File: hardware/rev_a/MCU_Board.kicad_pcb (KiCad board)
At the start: 2 copper layers, 30 x 55 mm, 28 parts, among them J1 ST-Link, J2 Conn_01x08, J3 Bus, J4 Conn_01x08, J5 Conn_02x07_Odd_Even, SW1 nRST, U1 STM32F042K6Tx, U3 SN65HVD230, U4 LP2985-3.3, Y1 8Mhz

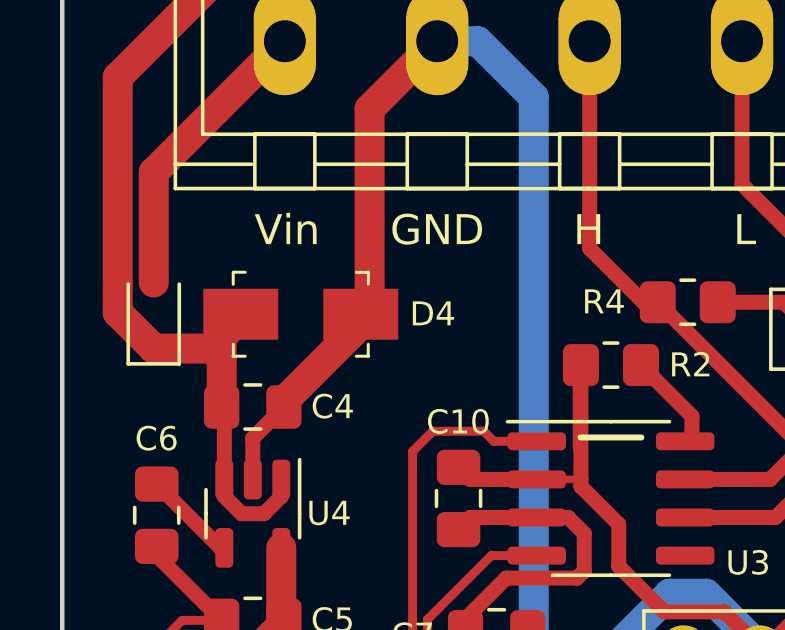
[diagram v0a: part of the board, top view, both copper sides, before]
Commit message: Remove the dependancy with external libraries, the TVS diode is now using the default symbol and a custom footprint
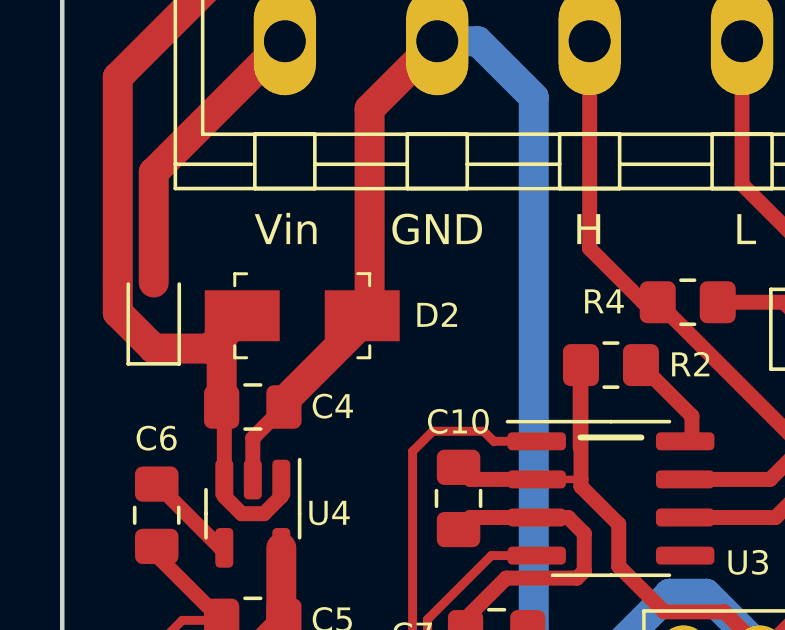
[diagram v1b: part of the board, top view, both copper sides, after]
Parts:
- removed D4: SMBJ12CA-E3/52, custom:DO-214AA
- added D2: SMBJ12CA-E3/52, custom:DO-214AA, F.Cu at (74.2, 113.2)
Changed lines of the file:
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@@
     )
-  )
-  (footprint "custom:DO-214AA" (layer "F.Cu")
-    (at 74.2 113.2)
-    (property "Sheetfile" "MCU_Board.kicad_sch")
-    (property "Sheetname" "")
-    (property "ki_description" "TVS DIODE 3.3V 14.1V SOD523")
-    (property "ki_keywords" "ESD5Z3.3T1GOSCT-ND")
-    (attr smd)
-    (fp_text reference "D4" (at 4.4 0) (layer "F.SilkS")
-        (effects (font (size 0.8 0.8) (thickness 0.15)))
-    )
-    (fp_text value "SMBJ12CA-E3/52" (at 0 2.45) (layer "F.Fab")
-        (effects (font (size 1 1) (thickness 0.15)))
-    )
-    (fp_text user "${REFERENCE}" (at 0.40894 0) (layer "F.Fab")
-        (effects (font (size 0.75 0.75) (thickness 0.075)))
-    )
-    (fp_line (start -2.25 -1.4) (end -2.25 -1)
-      (stroke (width 0.1) (type solid)) (layer "F.SilkS"))
-    (fp_line (start -2.25 -1.4) (end -1.85 -1.4)
-      (stroke (width 0.1) (type solid)) (layer "F.SilkS"))
-    (fp_line (start -2.25 1.4) (end -2.25 1)
-      (stroke (width 0.1) (type solid)) (layer "F.SilkS"))
-    (fp_line (start -2.25 1.4) (end -1.85 1.4)
-      (stroke (width 0.1) (type solid)) (layer "F.SilkS"))
-    (fp_line (start 2.25 -1.4) (end 1.85 -1.4)
-      (stroke (width 0.1) (type solid)) (layer "F.SilkS"))
-    (fp_line (start 2.25 -1.4) (end 2.25 -1)
-      (stroke (width 0.1) (type solid)) (layer "F.SilkS"))
-    (fp_line (start 2.25 1.4) (end 1.85 1.4)
-      (stroke (width 0.1) (type solid)) (layer "F.SilkS"))
-    (fp_line (start 2.25 1.4) (end 2.25 1)
-      (stroke (width 0.1) (type solid)) (layer "F.SilkS"))
-    (fp_line (start -3.5 -1.55) (end -3.5 1.55)
-      (stroke (width 0.05) (type solid)) (layer "F.CrtYd"))
-    (fp_line (start -3.5 -1.55) (end 3.5 -1.55)
-      (stroke (width 0.05) (type solid)) (layer "F.CrtYd"))
-    (fp_line (start -3.5 1.55) (end 3.5 1.55)
-      (stroke (width 0.05) (type solid)) (layer "F.CrtYd"))
-    (fp_line (start 3.5 -1.55) (end 3.5 1.55)
-      (stroke (width 0.05) (type solid)) (layer "F.CrtYd"))
-    (fp_line (start -2.15 -1.3) (end 2.15 -1.3)
-      (stroke (width 0.1) (type solid)) (layer "F.Fab"))
-    (fp_line (start -2.15 1.3) (end 2.15 1.3)
-      (stroke (width 0.1) (type solid)) (layer "F.Fab"))
-    (fp_line (start -1.44018 1.30048) (end -1.36398 1.30048)
-      (stroke (width 0.1) (type solid)) (layer "F.Fab"))
-    (fp_line (start -1.36144 -1.30048) (end -1.44018 -1.30048)
-      (stroke (width 0.1) (type solid)) (layer "F.Fab"))
-    (pad "A" smd rect (at 2 0) (size 2.5 1.7) (layers "F.Cu" "F.Paste" "F.Mask")
-      (net 1 "GND") (pintype "bidirectional"))
-    (pad "K" smd rect (at -2 0) (size 2.5 1.7) (layers "F.Cu" "F.Paste" "F.Mask")
-      (net 3 "/VIN") (pintype "bidirectional"))
   )
   (footprint "Diode_SMD:D_SOD-323F" (layer "F.Cu")
@@
     )
   )
+  (footprint "custom:DO-214AA" (layer "F.Cu")
+    (at 74.25 113.25 180)
+    (property "Sheetfile" "MCU_Board.kicad_sch")
+    (property "Sheetname" "")
+    (property "ki_description" "Bidirectional transient-voltage-suppression diode")
+    (property "ki_keywords" "diode TVS thyrector")
+    (attr smd)
+    (fp_text reference "D2" (at -4.5 0) (layer "F.SilkS")
+        (effects (font (size 0.8 0.8) (thickness 0.15)))
+    )
+    (fp_text value "SMBJ12CA-E3/52" (at 0 2.45) (layer "F.Fab")
+        (effects (font (size 1 1) (thickness 0.15)))
+    )
+    (fp_text user "${REFERENCE}" (at 0.40894 0) (layer "F.Fab")
+        (effects (font (size 0.75 0.75) (thickness 0.075)))
+    )
+    (fp_line (start -2.25 -1.4) (end -2.25 -1)
+      (stroke (width 0.1) (type solid)) (layer "F.SilkS"))
+    (fp_line (start -2.25 -1.4) (end -1.85 -1.4)
+      (stroke (width 0.1) (type solid)) (layer "F.SilkS"))
+    (fp_line (start -2.25 1.4) (end -2.25 1)
+      (stroke (width 0.1) (type solid)) (layer "F.SilkS"))
+    (fp_line (start -2.25 1.4) (end -1.85 1.4)
+      (stroke (width 0.1) (type solid)) (layer "F.SilkS"))
+    (fp_line (start 2.25 -1.4) (end 1.85 -1.4)
+      (stroke (width 0.1) (type solid)) (layer "F.SilkS"))
+    (fp_line (start 2.25 -1.4) (end 2.25 -1)
+      (stroke (width 0.1) (type solid)) (layer "F.SilkS"))
+    (fp_line (start 2.25 1.4) (end 1.85 1.4)
+      (stroke (width 0.1) (type solid)) (layer "F.SilkS"))
+    (fp_line (start 2.25 1.4) (end 2.25 1)
+      (stroke (width 0.1) (type solid)) (layer "F.SilkS"))
+    (fp_line (start -3.5 -1.55) (end -3.5 1.55)
+      (stroke (width 0.05) (type solid)) (layer "F.CrtYd"))
+    (fp_line (start -3.5 -1.55) (end 3.5 -1.55)
+      (stroke (width 0.05) (type solid)) (layer "F.CrtYd"))
+    (fp_line (start -3.5 1.55) (end 3.5 1.55)
+      (stroke (width 0.05) (type solid)) (layer "F.CrtYd"))
+    (fp_line (start 3.5 -1.55) (end 3.5 1.55)
+      (stroke (width 0.05) (type solid)) (layer "F.CrtYd"))
+    (fp_line (start -2.15 -1.3) (end 2.15 -1.3)
+      (stroke (width 0.1) (type solid)) (layer "F.Fab"))
+    (fp_line (start -2.15 1.3) (end 2.15 1.3)
+      (stroke (width 0.1) (type solid)) (layer "F.Fab"))
+    (fp_line (start -1.44018 1.30048) (end -1.36398 1.30048)
+      (stroke (width 0.1) (type solid)) (layer "F.Fab"))
+    (fp_line (start -1.36144 -1.30048) (end -1.44018 -1.30048)
+      (stroke (width 0.1) (type solid)) (layer "F.Fab"))
+    (pad "1" smd rect (at -2 0 180) (size 2.5 1.7) (layers "F.Cu" "F.Paste" "F.Mask")
+      (net 1 "GND") (pinfunction "A1") (pintype "passive"))
+    (pad "2" smd rect (at 2 0 180) (size 2.5 1.7) (layers "F.Cu" "F.Paste" "F.Mask")
+      (net 3 "/VIN") (pinfunction "A2") (pintype "passive"))
+  )
   (footprint "Connector_PinHeader_2.54mm:PinHeader_1x02_P2.54mm_Vertical" (layer "F.Cu")

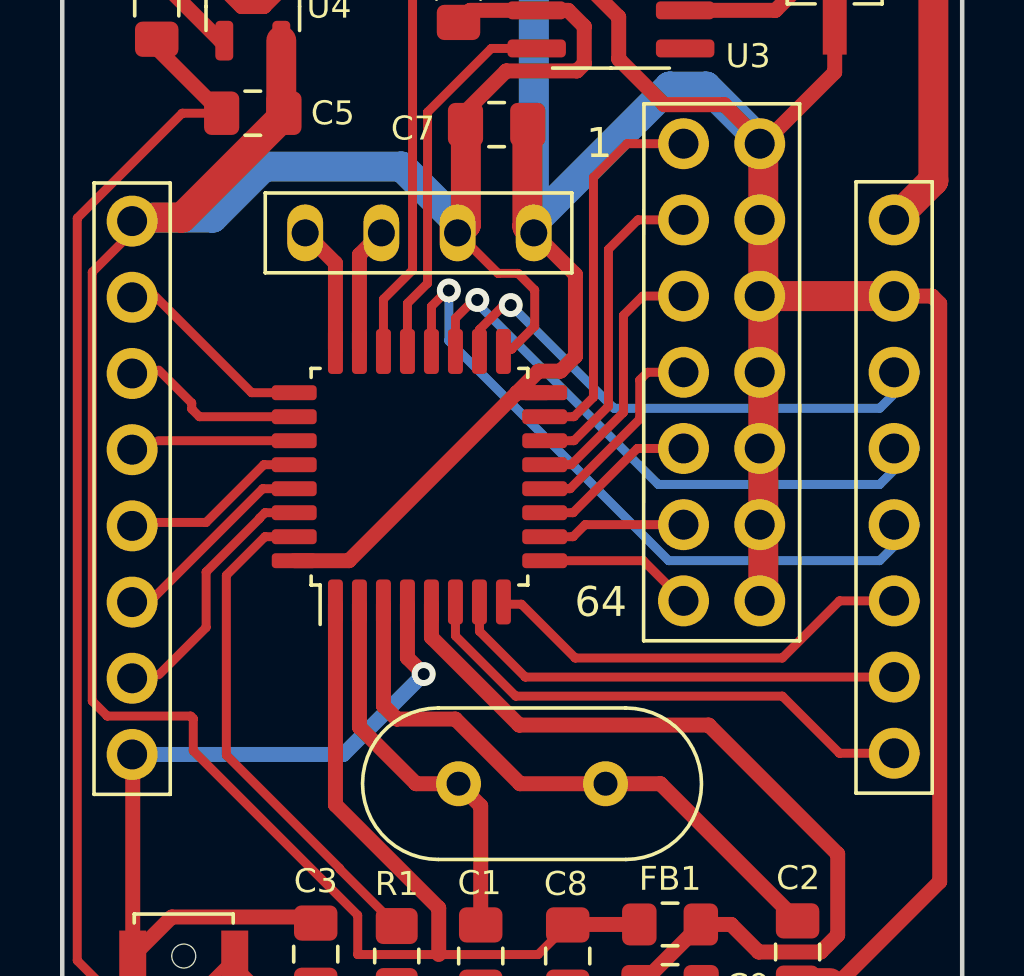
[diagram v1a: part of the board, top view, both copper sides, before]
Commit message: Update the reference of the input connector
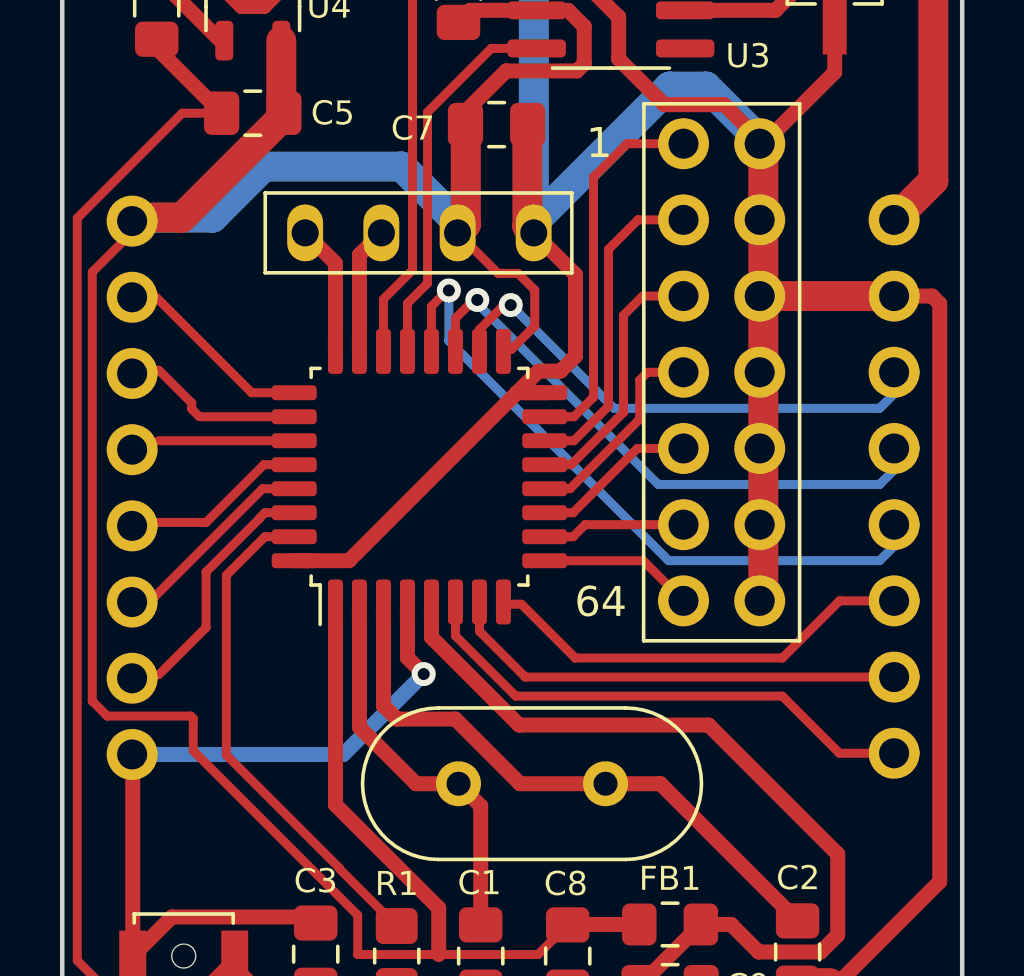
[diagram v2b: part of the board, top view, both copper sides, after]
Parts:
- J2, J4: moved to B.Cu
- turned J2 to 180 degrees
- turned J4 to 180 degrees

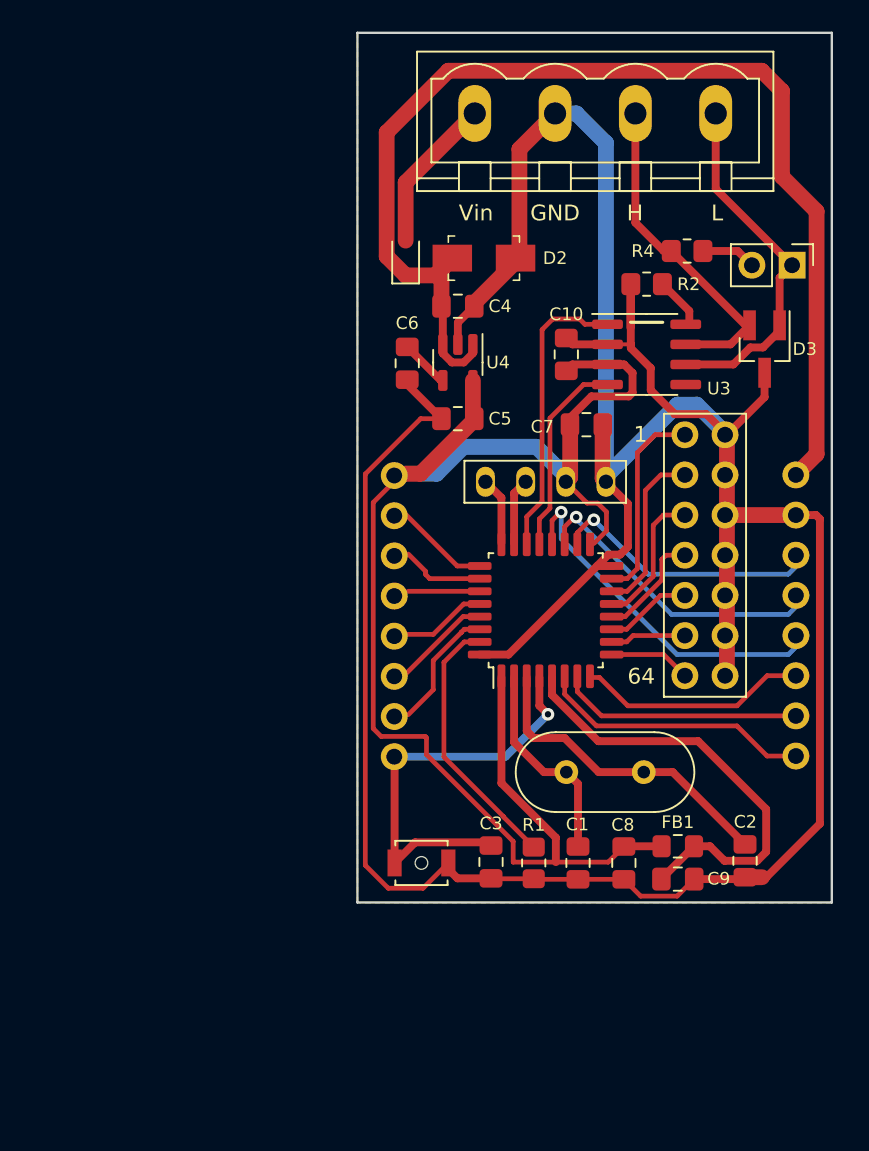
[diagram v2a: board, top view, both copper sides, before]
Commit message: Refactorisation de l'étage d'entrée en utilisant un régulateur à découpage DC/DC type buck
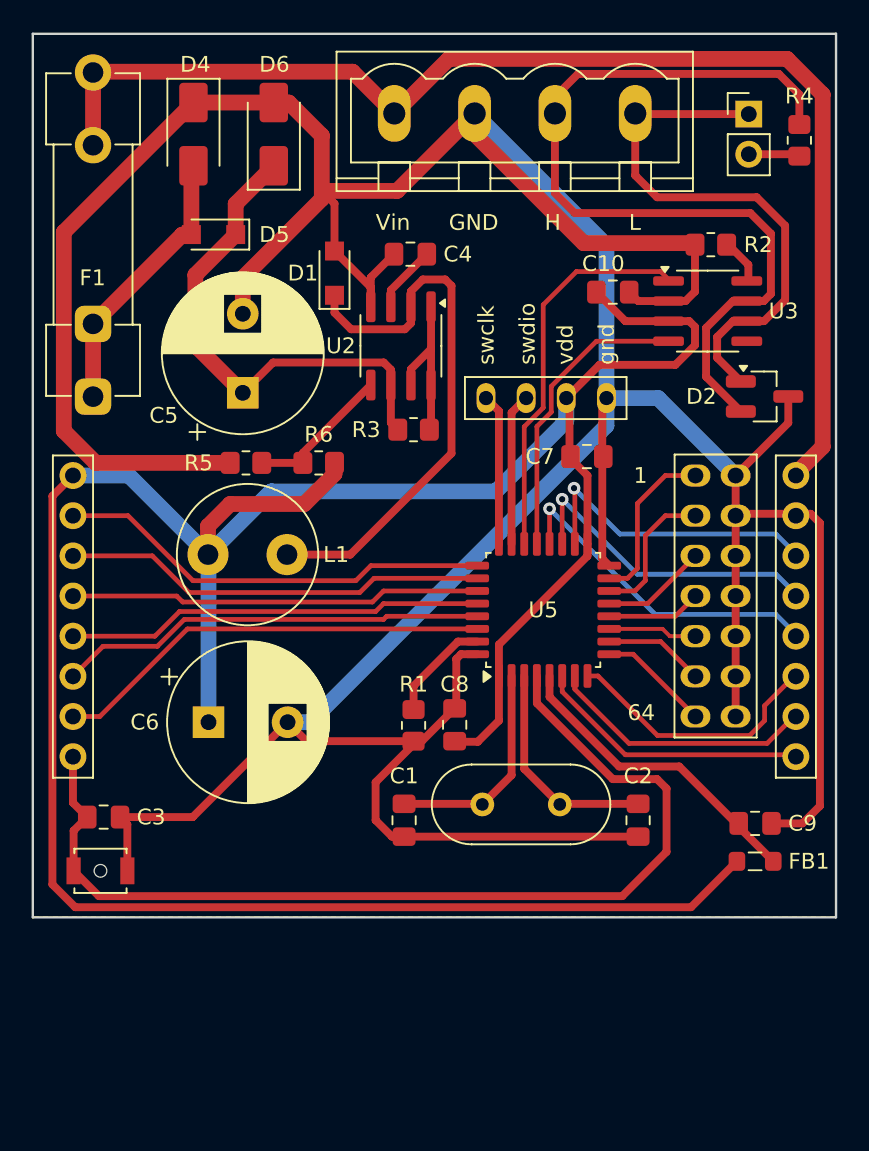
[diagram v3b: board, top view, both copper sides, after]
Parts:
- removed D3: SM24CANB-02HTG, Package_TO_SOT_SMD:SOT-23_Handsoldering
- removed U1: STM32F042K6Tx, Package_QFP:LQFP-32_7x7mm_P0.8mm
- removed U4: LP2985-3.3, Package_TO_SOT_SMD:SOT-23-5
- added D4: SMAJ33CA, Diode_SMD:D_SMA, F.Cu at (55.9, 105.4)
- added D5: PMEG6020CER, Diode_SMD:Nexperia_CFP3_SOD-123W, F.Cu at (57.1, 111.8)
- added D6: SMAJ4750A, Diode_SMD:D_SMA, F.Cu at (61.0, 105.4)
- added F1: Fuse, Fuse:Fuseholder_Clip-5x20mm_Littelfuse_100_Inline_P20.50x4.60mm_D1.30mm_Horizontal, F.Cu at (49.5, 122.0)
- added L1: 470u, Inductor_THT:L_Radial_D8.7mm_P5.00mm_Fastron_07HCP, F.Cu at (61.8, 132.0)
- added R3: 0R47, Resistor_SMD:R_0805_2012Metric_Pad1.20x1.40mm_HandSolder, F.Cu at (69.8, 124.1)
- added R5: 10k, Resistor_SMD:R_0805_2012Metric_Pad1.20x1.40mm_HandSolder, F.Cu at (59.2, 126.2)
- added R6: 6k2, Resistor_SMD:R_0805_2012Metric_Pad1.20x1.40mm_HandSolder, F.Cu at (63.8, 126.2)
- added U2: MC34063AD, Package_SO:SOIC-8_3.9x4.9mm_P1.27mm, F.Cu at (69.0, 118.8)
- added U5: STM32F042K6Tx, Package_QFP:LQFP-32_7x7mm_P0.8mm, F.Cu at (78.0, 135.5)
- C4: value 2u2 -> 470p
- C5: value 2u2 -> 100u; footprint Capacitor_SMD:C_0805_2012Metric_Pad1.18x1.45mm_HandSolder -> Capacitor_THT:CP_Radial_D10.0mm_P5.00mm
- C6: value 10n -> 1000u; footprint Capacitor_SMD:C_0805_2012Metric_Pad1.18x1.45mm_HandSolder -> Capacitor_THT:CP_Radial_D10.0mm_P5.00mm
- D1: value PMEG3020EJ,115 -> PMEG4020CERX; footprint Diode_SMD:D_SOD-323F -> Diode_SMD:Nexperia_CFP3_SOD-123W
- D2: value SMBJ12CA-E3/52 -> SM24CANB-02HTG; footprint custom:DO-214AA -> Package_TO_SOT_SMD:SOT-23_Handsoldering
- FB1: value Ferrite_Bead -> FerriteBead; footprint Inductor_SMD:L_0805_2012Metric_Pad1.15x1.40mm_HandSolder -> Inductor_SMD:L_0805_2012Metric_Pad1.05x1.20mm_HandSolder
- J2, J4: moved to F.Cu
- moved C6 25.9 mm to (56.8, 142.6), turned to 0 degrees
- moved C3 24.7 mm to (50.2, 148.6), turned to 0 degrees
- moved J2 20.3 mm to (48.3, 127.0), turned to 0 degrees
- moved SW1 20.3 mm to (50.0, 152.0)
- moved D2 19.8 mm to (92.0, 122.0), turned to 0 degrees
- moved C8 13.8 mm to (72.4, 142.8), turned to 90 degrees
- moved C5 13.7 mm to (59.0, 121.8), turned to 90 degrees
- moved R1 11.6 mm to (69.8, 142.8)
- moved C1 11.3 mm to (69.2, 148.8)
- moved R4 9.97 mm to (94.2, 105.8), turned to -90 degrees
- moved JP1 9.94 mm to (91.0, 104.1), turned to 0 degrees
- moved C2 7.23 mm to (84.0, 148.8)
- moved C9 6.02 mm to (91.4, 149.0)
- moved Y1 5.69 mm to (74.2, 147.8)
- moved J1 5.29 mm to (82.0, 122.1)
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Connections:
- C4 pad 1: /VIN -> Net-(U2-TC)
- C5 pad 1: GND -> Net-(D5-K)
- C5 pad 2: /VDD -> GND
- C6 pad 1: Net-(U4-BP) -> /VDD
- D1 pad 1: /VIN -> Net-(D1-K)
- D1 pad 2: Net-(D1-A) -> GND
- D2 pad 1: GND -> /CAN_L
- D2 pad 2: /VIN -> /CAN_H
- FB1 pad 1: /VDDA -> /VDD
- FB1 pad 2: /VDD -> /VDDA
- J3 pad 4: Net-(D1-A) -> /VIN
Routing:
- net /VDD: track 93.3 -> 176.6 mm
- net GND: track 207.9 -> 285.5 mm
- net /nRST: track 25.3 -> 63.4 mm, vias 1 -> 0
- net Net-(D1-K): track 0.00 -> 35.2 mm
- net /CAN_H: track 21.1 -> 54.2 mm
- net Net-(D5-K): track 0.00 -> 32.0 mm
- net /PB3: track 5.20 -> 26.9 mm
- net /PA15: track 6.01 -> 27.7 mm
- net /PB4: track 4.46 -> 26.0 mm
- net /PB6: track 6.16 -> 27.1 mm
- net /PB5: track 5.44 -> 26.4 mm
- net /PB7: track 7.77 -> 28.2 mm
- net Net-(D4-A2): track 0.00 -> 17.6 mm
- net /CAN_L: track 22.3 -> 35.3 mm
- net Net-(U2-DC): track 0.00 -> 10.6 mm
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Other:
- board size 30 x 55 mm -> 50.8 x 55.9 mm
- board text added: "gnd"
- board text added: "swclk"
- board text added: "swdio"
- board text added: "vdd"
